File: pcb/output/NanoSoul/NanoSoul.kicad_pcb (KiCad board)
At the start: 2 copper layers, 108 x 108 mm, 57 parts, among them J1 JST_PH_B2B-PH-K_1x02_P2.00mm_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, J2 PinHeader_1x02_P2.54mm_Vertic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, J3 PinHeader_1x20_P2.54mm_Vertic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, J4 PinHeader_1x20_P2.54mm_Vertic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, J5 PinHeader_1x06_P2.54mm_Vertic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, J6 PinHeader_1x06_P2.54mm_Vertic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, J7 PinHeader_1x06_P2.54mm_Vertic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, J8 JST_SH_BM04B-SRSS-TB_1x04-1MP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, Q1 SOT-23-6_L2.9-W1.6-P0.95-LS2.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, SW1 SW_SPST_CK_RS282G05A3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

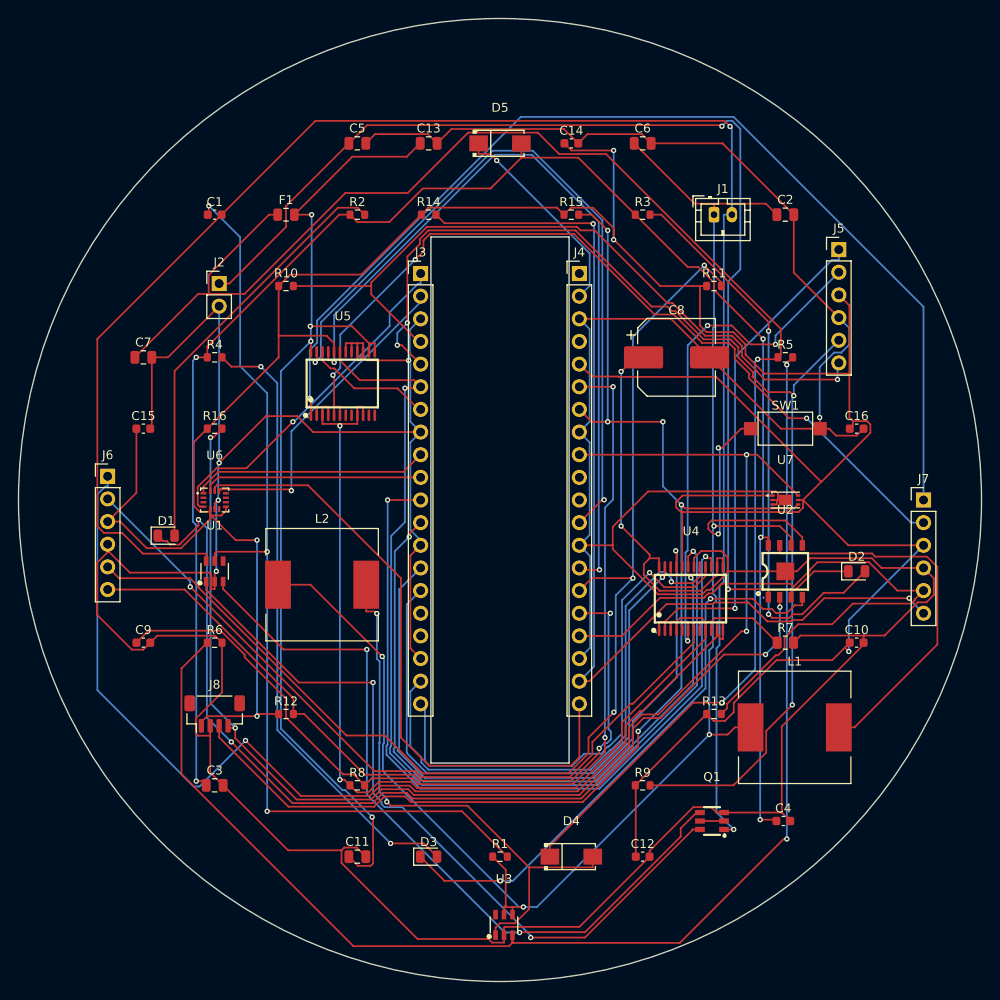
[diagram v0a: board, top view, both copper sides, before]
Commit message: pcb: 3mm 白边 + J2/J7 离 J4 + DRC 丝印告警清零
- 最外围 3mm 白边：板放大到 94×92（Ø108 切边收小到 7/8mm），铜/器件焊盘距最外缘 ≥3mm
  （自动布线内缩 3mm；顶排 J5/J6 下移、J8 左移退出白边区）。
- J2/J7 离 J4：右月牙整体右移 1.6mm，离 J4 本体 +0.83mm（原相擦 0.78mm）。
- DRC = 0 warning：5 个位号(D4/D5/Q1/U1/U7)挪开、接线图例升到 0.8mm 并缩短、
  删 J3/J4 压挖孔丝印、隐藏 6 安装孔与 U7 位号。
- 17.8mm 母座行距核对通过；4 个 M3 安装孔成规则 54×82 矩形（旧版钉在 Ø108 圆外、钻不出，已修正）。
- 余 MOT_RTN/GND 各 1 段跨挖孔大电流网/地：按 docs 铁律出板前人工绕挖孔补（GND 建议铺地铜），
  网表连接关系正确（其余 170 网 0 短路）。原理图 ERC 不适用：circuit-synth 开源导出无导线、
  网表为真值源。详见 docs/05 §9.1。
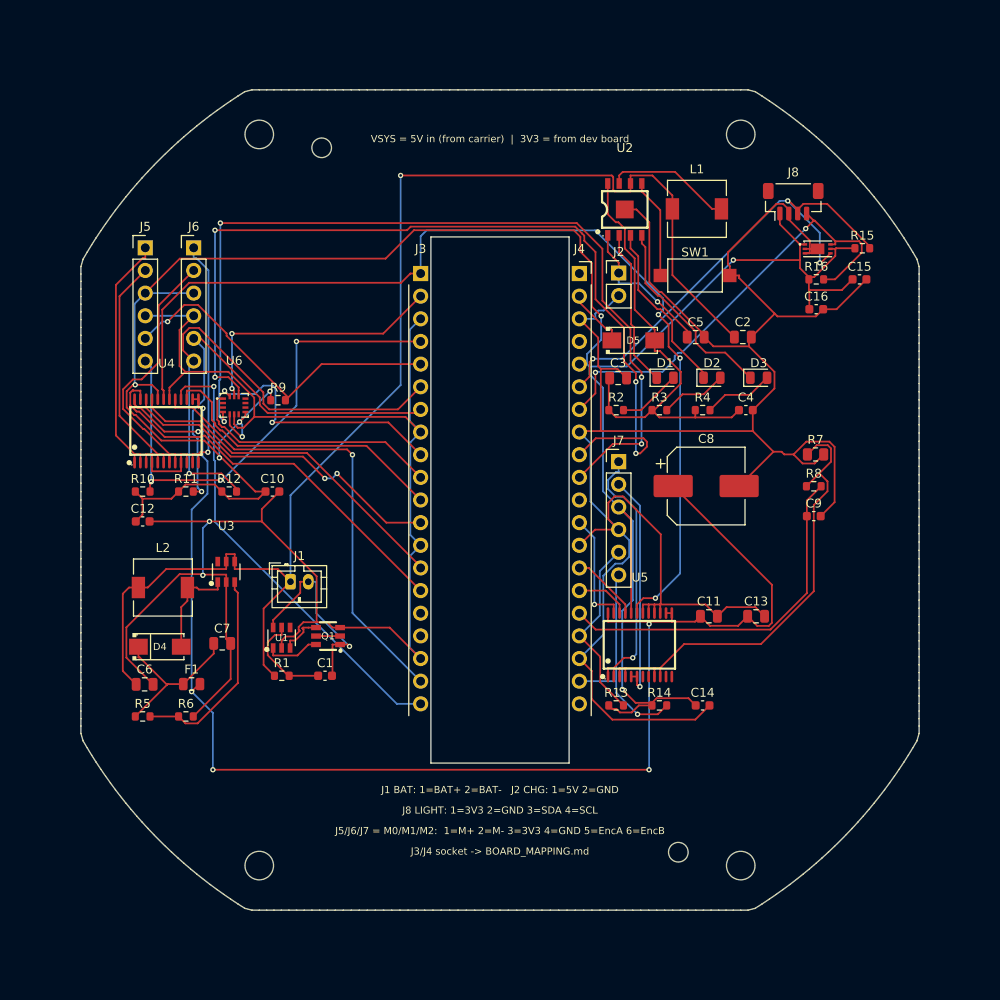
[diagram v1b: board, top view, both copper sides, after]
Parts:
- added H1: MountingHole_3.2mm_M3, MountingHole_3.2mm_M3, F.Cu at (123.0, 59.0)
- added H2: MountingHole_3.2mm_M3, MountingHole_3.2mm_M3, F.Cu at (177.0, 59.0)
- added H3: MountingHole_3.2mm_M3, MountingHole_3.2mm_M3, F.Cu at (123.0, 141.0)
- added H4: MountingHole_3.2mm_M3, MountingHole_3.2mm_M3, F.Cu at (177.0, 141.0)
- added H5: MountingHole_2.2mm_M2, MountingHole_2.2mm_M2, F.Cu at (130.0, 60.5)
- added H6: MountingHole_2.2mm_M2, MountingHole_2.2mm_M2, F.Cu at (170.0, 139.5)
- J3, J4: value PinHeader_1x20_P2.54mm_Vertical -> PinSocket_1x20_P2.54mm_Vertical; footprint PinHeader_1x20_P2.54mm_Vertical -> PinSocket_1x20_P2.54mm_Vertical
- L1, L2: value L_12x12mm_H8mm -> L_6.3x6.3_H3; footprint L_12x12mm_H8mm -> L_6.3x6.3_H3
- moved J8 86.7 mm to (182.9, 66.5)
- moved R5 82.6 mm to (109.9, 124.3)
- moved C6 82.5 mm to (110.1, 120.7)
- moved C15 82.0 mm to (190.3, 75.3)
- moved J5 77.8 mm to (110.2, 71.7)
- moved C9 76.5 mm to (185.2, 101.8)
- moved R16 69.5 mm to (185.5, 75.3)
- moved C10 67.7 mm to (124.5, 99.1)
- moved C12 67.5 mm to (109.9, 102.4)
- moved D3 65.2 mm to (179.0, 86.3)
- moved C14 64.7 mm to (172.7, 123.0)
- moved C13 64.5 mm to (178.7, 113.0)
- moved C3 64.3 mm to (163.2, 86.3)
- moved R11 63.6 mm to (114.8, 99.1)
- moved J1 62.9 mm to (126.5, 109.2)
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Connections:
- J3 pad 1: IMU_INT -> MOTOR_STBY
- J3 pad 10: IMU_MOSI -> IMU_MISO
- J3 pad 2: IMU_CS -> IMU_SCLK
- J3 pad 6: MOTOR_STBY -> M1_ENC_B
- J3 pad 7: M2_IN2 -> M1_ENC_A
- J3 pad 9: IMU_MISO -> IMU_MOSI
- J4 pad 10: P4_GPIO23 -> IMU_INT
- J4 pad 15: M1_ENC_A -> M2_IN2
- J4 pad 16: M1_ENC_B -> MOT_ISENSE
- J4 pad 20: IMU_SCLK -> P4_GPIO23
- J4 pad 6: MOT_ISENSE -> I2C1_SDA
- J4 pad 7: I2C1_SDA -> I2C1_SCL
- J4 pad 9: I2C1_SCL -> IMU_CS
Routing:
- net CELL_MINUS: track 198.7 -> 22.5 mm, vias 2 -> 1
- net VMOT: track 177.7 -> 18.5 mm, vias 2 -> 0
- net V5: track 191.6 -> 51.2 mm, vias 5 -> 0
- net MT_FB: track 152.8 -> 23.5 mm, vias 2 -> 0
- net GND: track 556.5 -> 432.8 mm, vias 5 -> 2
- net CHG_IN: track 125.4 -> 16.5 mm, vias 2 -> 1
- net I2C1_SCL: track 153.4 -> 51.7 mm, vias 4 -> 2
- net V3V3: track 367.6 -> 269.0 mm, vias 5 -> 8
- net DW_VCC: track 107.5 -> 10.8 mm, vias 3 -> 0
- net IP_LED1: track 111.4 -> 17.7 mm, vias 4 -> 0
- net M0_ENC_A: track 131.7 -> 38.9 mm, vias 4 -> 1
- net M2_OUT_A: track 120.6 -> 29.8 mm
- net M2_ENC_B: track 115.0 -> 24.5 mm, vias 2 -> 1
- net M1_OUT_A: track 117.0 -> 27.5 mm
- net I2C1_SDA: track 143.0 -> 55.5 mm, vias 5 -> 3
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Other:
- board size 108 x 108 mm -> 94 x 92 mm
- board text added: "J1 BAT: 1=BAT+ 2=BAT- J2 CHG: 1=5V 2=GND"
- board text added: "J3/J4 socket -> BOARD_MAPPING.md"
- board text added: "J5/J6/J7 = M0/M1/M2: 1=M+ 2=M- 3=3V3 4=GND 5=EncA 6=EncB"
- board text added: "J8 LIGHT: 1=3V3 2=GND 3=SDA 4=SCL"
- board text added: "VSYS = 5V in (from carrier) | 3V3 = from dev board"

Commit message: pcb: 自写迷宫布线补通 MOT_RTN/GND → PCB 0 未连 / 0 DRC
- Freerouting 留空的 2 条跨挖孔大电流网/地（两端被母座+月牙器件夹死），用带净空校验的
  双层迷宫布线器(route2.py)布通：多源 BFS + 端点吸附/打过孔 + 守 3mm 白边 + 绕挖孔。
- 复核：kicad-cli pcb drc = 0 violations / 0 unconnected；新铜距外缘 ≥3mm（5mm）。
- 至此：PCB DRC 0、原理图 ERC 0（网表为真值源已核对）、3mm 白边、J2/J7 离 J4、17.8 行距 全过。
- MOT_RTN 暂 0.5mm，载大电流前在 GUI 加宽；docs/05 §9.1 更新。
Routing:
- net MOT_RTN: track 62.4 -> 161.8 mm, vias 0 -> 2
- net GND: track 432.8 -> 482.3 mm, vias 2 -> 4
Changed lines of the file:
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@@
 	)
 	(segment
+		(start 160.25 121)
+		(end 160.25 119.25)
+		(width 0.5)
+		(layer "F.Cu")
+		(net "GND")
+	)
+	(segment
 		(start 161.0131 84.9985)
 		(end 161.0131 81.7931)
@@
 	)
 	(segment
+		(start 137.75 114.25)
+		(end 137.75 129.5)
+		(width 0.5)
+		(layer "F.Cu")
+		(net "GND")
+	)
+	(segment
 		(start 119.795 116.085)
 		(end 119.795 120.08)
@@
 	)
 	(via
+		(at 137.75 129.5)
+		(size 0.6)
+		(drill 0.3)
+		(layers "F.Cu" "B.Cu")
+		(net "GND")
+	)
+	(via
 		(at 116.6775 108.445)
 		(size 0.6)
@@
 		(net "GND")
 	)
+	(via
+		(at 160.25 121)
+		(size 0.6)
+		(drill 0.3)
+		(layers "F.Cu" "B.Cu")
+		(net "GND")
+	)
 	(segment
 		(start 160.6866 79.1055)
@@
 	)
 	(segment
+		(start 160.25 123.75)
+		(end 160.25 121)
+		(width 0.5)
+		(layer "B.Cu")
+		(net "GND")
+	)
+	(segment
 		(start 161.6471 78.7529)
 		(end 161.0392 78.7529)
@@
 	)
 	(segment
+		(start 160 124)
+		(end 160 123.75)
+		(width 0.5)
+		(layer "B.Cu")
+		(net "GND")
+	)
+	(segment
 		(start 163.315 77.085)
 		(end 161.6471 78.7529)
@@
 	)
 	(segment
+		(start 158.5 130.25)
+		(end 158.5 124.25)
+		(width 0.5)
+		(layer "B.Cu")
+		(net "GND")
+	)
+	(segment
+		(start 158.5 124.25)
+		(end 159.75 124.25)
+		(width 0.5)
+		(layer "B.Cu")
+		(net "GND")
+	)
+	(segment
 		(start 164.4902 106.3621)
 		(end 164.4902 104.5032)
@@
 	)
 	(segment
+		(start 160 123.75)
+		(end 160.25 123.75)
+		(width 0.5)
+		(layer "B.Cu")
+		(net "GND")
+	)
+	(segment
 		(start 162.9502 107.133)
 		(end 163.7193 107.133)
@@
 	)
 	(segment
+		(start 159.75 124.25)
+		(end 159.75 124)
+		(width 0.5)
+		(layer "B.Cu")
+		(net "GND")
+	)
+	(segment
 		(start 160.6866 79.6037)
 		(end 160.7415 79.6585)
@@
 	)
 	(segment
+		(start 159.75 124)
+		(end 160 124)
+		(width 0.5)
+		(layer "B.Cu")
+		(net "GND")
+	)
+	(segment
 		(start 161.5916 115.0884)
 		(end 161.5916 108.4916)
@@
 	)
 	(segment
+		(start 137.75 129.5)
+		(end 137.75 130.25)
+		(width 0.5)
+		(layer "B.Cu")
+		(net "GND")
+	)
+	(segment
 		(start 139.9483 93.5317)
 		(end 139.9483 103.9283)
@@
 	)
 	(segment
+		(start 137.75 130.25)
+		(end 158.5 130.25)
+		(width 0.5)
+		(layer "B.Cu")
+		(net "GND")
+	)
+	(segment
 		(start 162.11 112.68)
 		(end 162.11 113.6437)
@@
 		(net "MOT_RTN")
 	)
+	(via
+		(at 114.2275 96.75)
+		(size 0.55)
+		(drill 0.3)
+		(layers "F.Cu" "B.Cu")
+		(net "MOT_RTN")
+	)
+	(via
+		(at 167.32 119.75)
+		(size 0.55)
+		(drill 0.3)
+		(layers "F.Cu" "B.Cu")
+		(net "MOT_RTN")
+	)
+	(segment
+		(start 114.2275 96.75)
+		(end 114.25 97)
+		(width 0.5)
+		(layer "B.Cu")
+		(net "MOT_RTN")
+	)
+	(segment
+		(start 114.25 97)
+		(end 114.25 131.25)
+		(width 0.5)
+		(layer "B.Cu")
+		(net "MOT_RTN")
+	)
+	(segment
+		(start 167.5 119.75)
+		(end 167.32 119.75)
+		(width 0.5)
+		(layer "B.Cu")
+		(net "MOT_RTN")
+	)
+	(segment
+		(start 167 131)
+		(end 167.5 131)
+		(width 0.5)
+		(layer "B.Cu")
+		(net "MOT_RTN")
+	)
+	(segment
+		(start 167.5 131)
+		(end 167.5 119.75)
+		(width 0.5)
+		(layer "B.Cu")
+		(net "MOT_RTN")
+	)
+	(segment
+		(start 114.25 131.25)
+		(end 167 131.25)
+		(width 0.5)
+		(layer "B.Cu")
+		(net "MOT_RTN")
+	)
+	(segment
+		(start 167 131.25)
+		(end 167 131)
+		(width 0.5)
+		(layer "B.Cu")
+		(net "MOT_RTN")
+	)

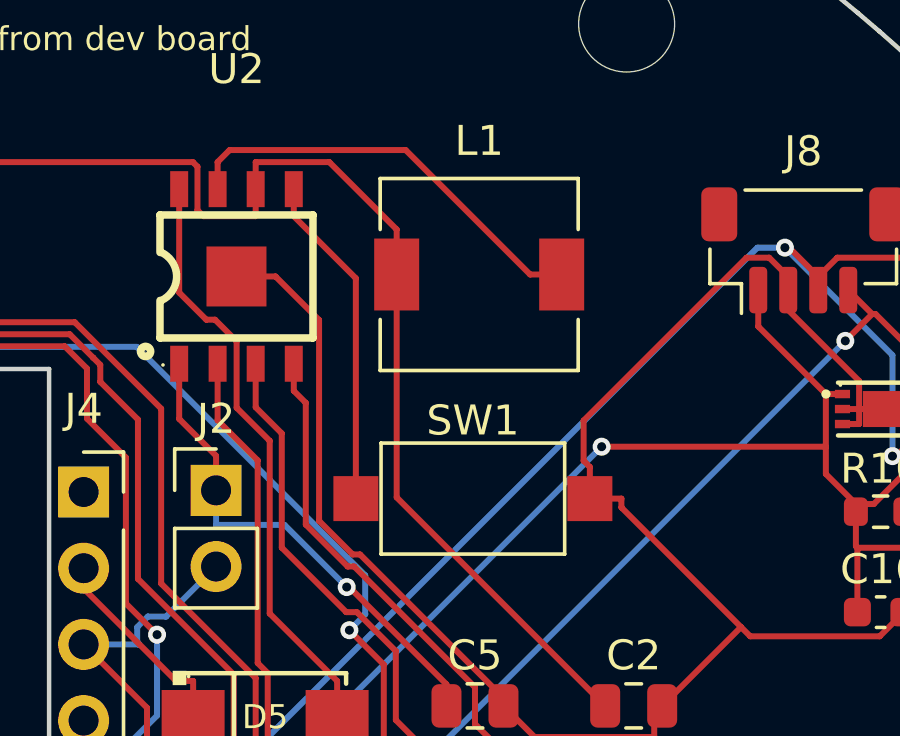
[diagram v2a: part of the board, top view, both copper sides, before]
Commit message: pcb: 料号确认补全 + SW1 换 C720477 + 电机轨 5.5V / DRC 0 ERC 0
待确认料号(report.xlsx)逐项查实并填进 fab BOM/CPL：
- C8→C4747956（原写 RYVP25V470UF8*10 查无此件，换 25V/470µF/8×10.5）
- L1→C2047296 / L2→C703091（LQH66SN 本体 6.3×6.3 与焊盘对得上；库存薄）
- J1→C131337 / J8→C495539(TBT版) / D1-3→C84256(红0805) / F1→C207025(0805L150)
- U2 C488349(认准 I²C 版) / U4U5 C141517(别买 C88224) 复核照原

板子改动并复验：
- SW1：C&K RS282G05A3 → TS-1088(C720477,2脚)；原 C318884(4脚)塞不进挤口袋、
  且查实其 KEY=pin1,2/GND=pin3,4(防接反)。新件右移0.8+上移1.0mm 避 VBAT，重布 KEY/GND
- R5 91k→82k：电机轨 MT3608 6.06→5.5V，给 F1 PTC 的 6V 耐压留余量
- DRC 0 违规/0 未连、ERC 0；3mm白边/母座17.80mm/挖孔15.5×59/6安装孔 均未受影响
- 重出 Gerber+钻孔/STEP/BOM/CPL；fab_bom_cpl 补 LCSC 映射，route2 加 __main__ 守卫便于复用
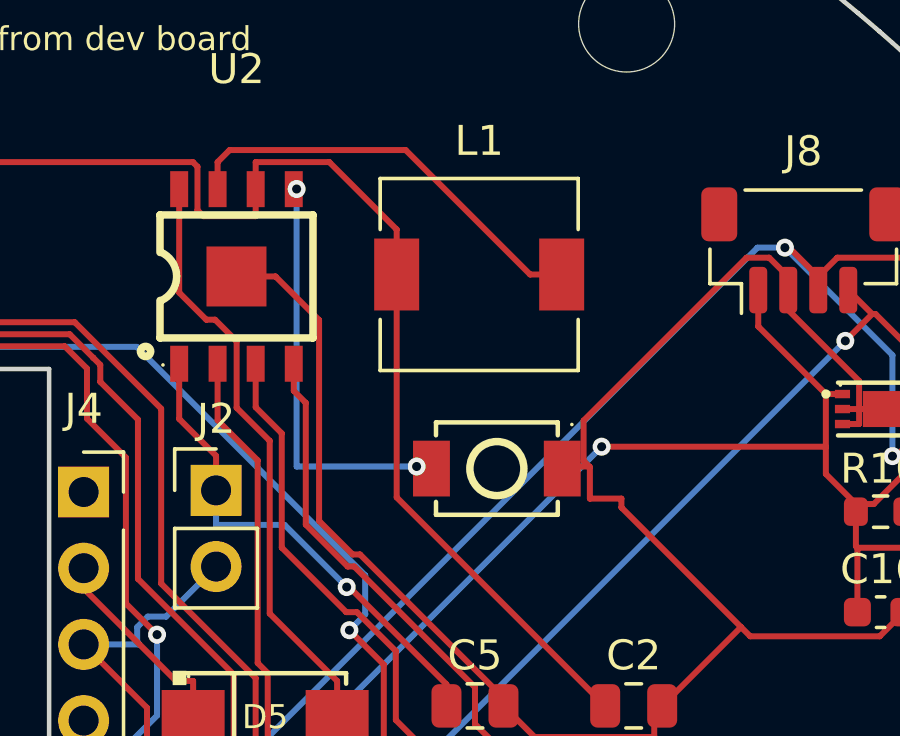
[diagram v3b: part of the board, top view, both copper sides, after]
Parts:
- R5: value R_0603_1608Metric -> 82k
- SW1: value SW_SPST_CK_RS282G05A3 -> SW-SMD_L3.9-W3.0-P4.45; footprint SW_SPST_CK_RS282G05A3 -> SW-SMD_L3.9-W3.0-P4.45
- moved SW1 1.28 mm to (172.7, 73.8)
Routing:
- net KEY_BTN: track 11.2 -> 13.8 mm, vias 0 -> 2
- net GND: track 482.3 -> 483.3 mm
